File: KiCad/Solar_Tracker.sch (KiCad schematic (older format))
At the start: 56 parts

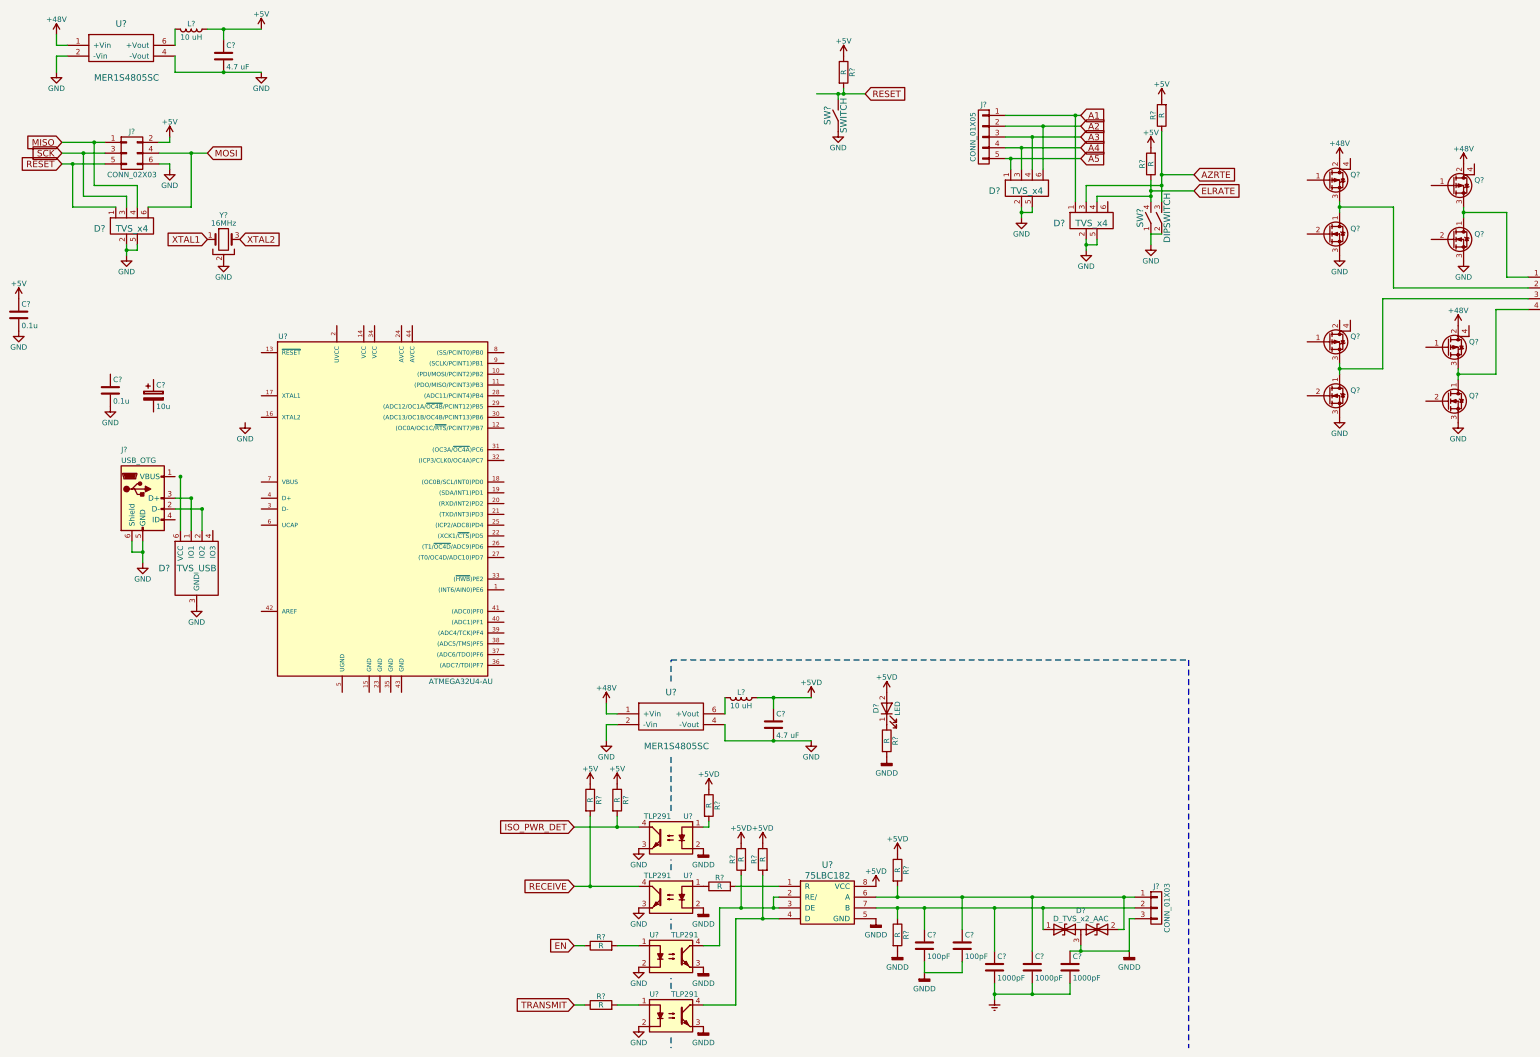
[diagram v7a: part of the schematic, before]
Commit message: Added USB hardware to ATMEGA32u4 symbol
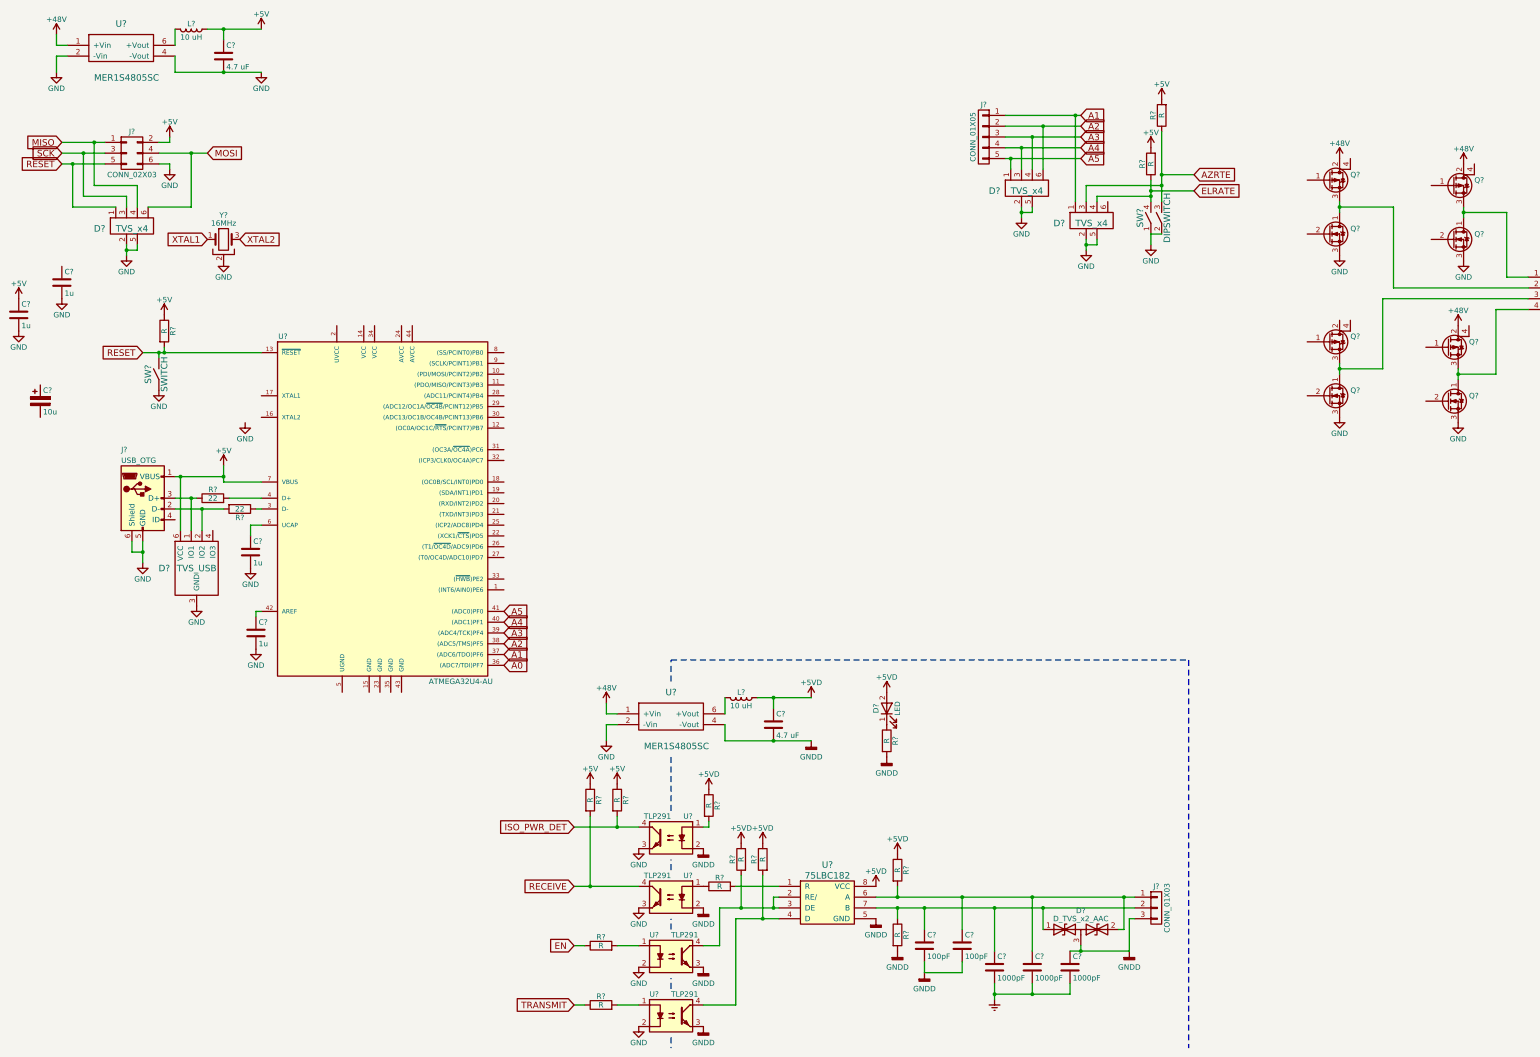
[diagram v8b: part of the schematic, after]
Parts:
- added C? (x2): 1u, symbol C
- added R? (x2): 22, symbol R
- C? (x2): value 0.1u -> 1u
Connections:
- net +5V: now also D?.6 (VCC), J?.1 (VBUS), U?.7 (VBUS)
- net A1: now also U?.37 ((ADC6/TDO)PF6)
- net A2: now also U?.38 ((ADC5/TMS)PF5)
- net A3: now also U?.39 ((ADC4/TCK)PF4)
- net A4: now also U?.40 ((ADC1)PF1)
- net A5: now also U?.41 ((ADC0)PF0)
- net GND: now also C?.2, C?.2; no longer C?.2, U?.4 (-Vout)
- net GNDD: now also C?.2, U?.4 (-Vout)
- net RESET: now also U?.13 (~RESET~)
- net at D?.2 (IO2), J?.2 (D-): now also R?.2
- net at D?.1 (IO1), J?.3 (D+): now also R?.1
- net at U?.3 (D-): now also R?.1
- net A0: now reaches U?.36 ((ADC7/TDI)PF7)
- net at U?.4 (D+): now also R?.2
- net at U?.42 (AREF): now also C?.1
- net at U?.6 (UCAP): now also C?.1
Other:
- moved on the sheet: C?, R?, SW?
